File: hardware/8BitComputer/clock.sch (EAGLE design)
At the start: 28 parts, among them IC1 LM555CN, J1 Power, J2 Power, Q1 P2N2222AZL1G, Q2 P2N2222AZL1G

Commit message: lay out for size of our FR-4 boards
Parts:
- added U$3: CMD_C0DE_LOGOCMD_CODE_LOGO_TOP_COPPER, logos:CMD_C0DE_LOGOCMD_CODE_LOGO_TOP_COPPER
- C2: device passives:C-USC0805 -> passives:C-US075-032X103
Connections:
- net GND: now also LED2.C; no longer R6.2
- net MANUAL_TIMER: now also R6.1; no longer LED2.A
- net N$5: now also LED2.A, R6.2; no longer LED2.C, R6.1
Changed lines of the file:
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@@
 <layers>
 <layer number="1" name="Top" color="4" fill="1" visible="no" active="no"/>
-<layer number="2" name="Route2" color="1" fill="3" visible="no" active="no"/>
-<layer number="3" name="Route3" color="4" fill="3" visible="no" active="no"/>
-<layer number="4" name="Route4" color="1" fill="4" visible="no" active="no"/>
-<layer number="5" name="Route5" color="4" fill="4" visible="no" active="no"/>
-<layer number="6" name="Route6" color="1" fill="8" visible="no" active="no"/>
-<layer number="7" name="Route7" color="4" fill="8" visible="no" active="no"/>
-<layer number="8" name="Route8" color="1" fill="2" visible="no" active="no"/>
-<layer number="9" name="Route9" color="4" fill="2" visible="no" active="no"/>
-<layer number="10" name="Route10" color="1" fill="7" visible="no" active="no"/>
-<layer number="11" name="Route11" color="4" fill="7" visible="no" active="no"/>
-<layer number="12" name="Route12" color="1" fill="5" visible="no" active="no"/>
-<layer number="13" name="Route13" color="4" fill="5" visible="no" active="no"/>
-<layer number="14" name="Route14" color="1" fill="6" visible="no" active="no"/>
-<layer number="15" name="Route15" color="4" fill="6" visible="no" active="no"/>
+<layer number="2" name="Route2" color="16" fill="1" visible="no" active="no"/>
+<layer number="3" name="Route3" color="17" fill="1" visible="no" active="no"/>
+<layer number="4" name="Route4" color="18" fill="1" visible="no" active="no"/>
+<layer number="5" name="Route5" color="19" fill="1" visible="no" active="no"/>
+<layer number="6" name="Route6" color="25" fill="1" visible="no" active="no"/>
+<layer number="7" name="Route7" color="26" fill="1" visible="no" active="no"/>
+<layer number="8" name="Route8" color="27" fill="1" visible="no" active="no"/>
+<layer number="9" name="Route9" color="28" fill="1" visible="no" active="no"/>
+<layer number="10" name="Route10" color="29" fill="1" visible="no" active="no"/>
+<layer number="11" name="Route11" color="30" fill="1" visible="no" active="no"/>
+<layer number="12" name="Route12" color="20" fill="1" visible="no" active="no"/>
+<layer number="13" name="Route13" color="21" fill="1" visible="no" active="no"/>
+<layer number="14" name="Route14" color="22" fill="1" visible="no" active="no"/>
+<layer number="15" name="Route15" color="23" fill="1" visible="no" active="no"/>
 <layer number="16" name="Bottom" color="1" fill="1" visible="no" active="no"/>
 <layer number="17" name="Pads" color="2" fill="1" visible="no" active="no"/>
 <layer number="18" name="Vias" color="2" fill="1" visible="no" active="no"/>
 <layer number="19" name="Unrouted" color="6" fill="1" visible="no" active="no"/>
-<layer number="20" name="Dimension" color="15" fill="1" visible="no" active="no"/>
+<layer number="20" name="Dimension" color="24" fill="1" visible="no" active="no"/>
 <layer number="21" name="tPlace" color="7" fill="1" visible="no" active="no"/>
 <layer number="22" name="bPlace" color="7" fill="1" visible="no" active="no"/>
@@
 <part name="U$1" library="passives" deviceset="SQUARE-TRIMPOT-POTENTIOMETER" device=""/>
 <part name="R2" library="passives" deviceset="RESISTOR" device="0805-RES" value="1 K"/>
-<part name="C2" library="passives" deviceset="C-US" device="C0805" value="100 nF"/>
+<part name="C2" library="passives" deviceset="C-US" device="075-032X103" value="100 nF"/>
 <part name="C3" library="passives" deviceset="C-US" device="C0805" value="1 uF"/>
 <part name="R3" library="passives" deviceset="RESISTOR" device="0805-RES" value="1 K"/>
@@
 <part name="J3" library="connector" deviceset="M08" device="SILK_FEMALE_PTH"/>
 <part name="J2" library="connector" deviceset="M02" device="PTH" value="Power"/>
+<part name="U$3" library="logos" deviceset="CMD_C0DE_LOGO" device="CMD_CODE_LOGO_TOP_COPPER"/>
 </parts>
 <sheets>
@@
 <attribute name="VALUE" x="39.116" y="56.769" size="1.778" layer="96"/>
 </instance>
-<instance part="LED2" gate="G$1" x="45.72" y="71.12" smashed="yes" rot="R180">
-<attribute name="NAME" x="42.164" y="75.692" size="1.778" layer="95" rot="R270"/>
-<attribute name="VALUE" x="50.165" y="75.692" size="1.778" layer="96" rot="R270"/>
-</instance>
-<instance part="R6" gate="G$1" x="45.72" y="83.82" smashed="yes" rot="R90">
-<attribute name="NAME" x="44.2214" y="80.01" size="1.778" layer="95" rot="R90"/>
-<attribute name="VALUE" x="49.022" y="80.01" size="1.778" layer="96" rot="R90"/>
+<instance part="LED2" gate="G$1" x="45.72" y="86.36" smashed="yes" rot="R180">
+<attribute name="NAME" x="42.164" y="90.932" size="1.778" layer="95" rot="R270"/>
+<attribute name="VALUE" x="50.165" y="90.932" size="1.778" layer="96" rot="R270"/>
+</instance>
+<instance part="R6" gate="G$1" x="45.72" y="73.66" smashed="yes" rot="R90">
+<attribute name="NAME" x="44.2214" y="69.85" size="1.778" layer="95" rot="R90"/>
+<attribute name="VALUE" x="49.022" y="69.85" size="1.778" layer="96" rot="R90"/>
 </instance>
 </instances>
@@
 <junction x="38.1" y="63.5"/>
 <label x="50.8" y="63.5" size="1.778" layer="95"/>
-<pinref part="LED2" gate="G$1" pin="A"/>
+<pinref part="R6" gate="G$1" pin="1"/>
 <wire x1="45.72" y1="63.5" x2="50.8" y2="63.5" width="0.1524" layer="91"/>
 <wire x1="45.72" y1="68.58" x2="45.72" y2="63.5" width="0.1524" layer="91"/>
@@
 </segment>
 <segment>
+<pinref part="LED2" gate="G$1" pin="C"/>
+<wire x1="45.72" y1="91.44" x2="45.72" y2="93.98" width="0.1524" layer="91"/>
+<label x="45.72" y="93.98" size="1.778" layer="95"/>
+</segment>
+</net>
+<net name="N$5" class="0">
+<segment>
 <pinref part="R6" gate="G$1" pin="2"/>
-<wire x1="45.72" y1="88.9" x2="45.72" y2="91.44" width="0.1524" layer="91"/>
-<label x="45.72" y="91.44" size="1.778" layer="95"/>
-</segment>
-</net>
-<net name="N$5" class="0">
-<segment>
-<pinref part="LED2" gate="G$1" pin="C"/>
-<pinref part="R6" gate="G$1" pin="1"/>
-<wire x1="45.72" y1="76.2" x2="45.72" y2="78.74" width="0.1524" layer="91"/>
+<pinref part="LED2" gate="G$1" pin="A"/>
+<wire x1="45.72" y1="78.74" x2="45.72" y2="83.82" width="0.1524" layer="91"/>
 </segment>
 </net>
@@
 </nets>
 </sheet>
+<sheet>
+<plain>
+</plain>
+<instances>
+<instance part="U$3" gate="G$1" x="40.64" y="63.5" smashed="yes"/>
+</instances>
+<busses>
+</busses>
+<nets>
+</nets>
+</sheet>

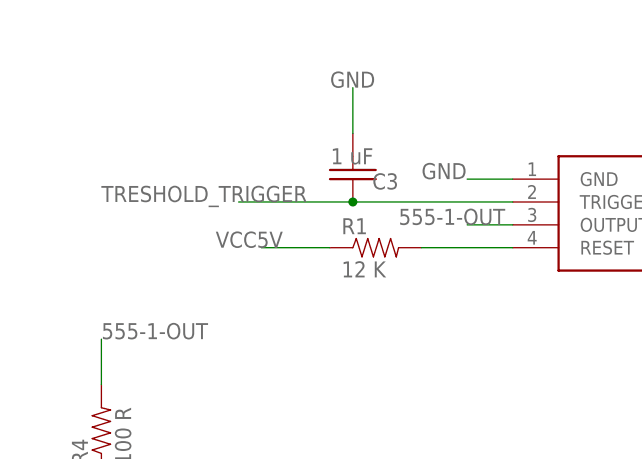
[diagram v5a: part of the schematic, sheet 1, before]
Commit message: fixed missing trace on 555- miss spelled threshold :(
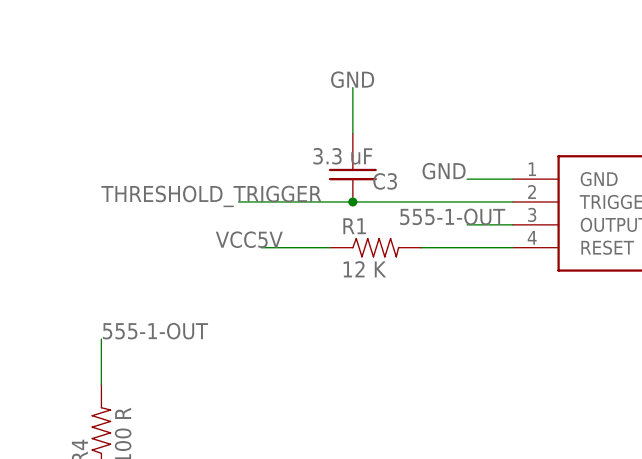
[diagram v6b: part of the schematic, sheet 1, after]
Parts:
- C3: value 1 uF -> 3.3 uF
- J3: value (none) -> CLK_OUTS
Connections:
- removed net TRESHOLD_TRIGGER: C3.1, IC1.TRIGGER
- net THRESHOLD_TRIGGER: now also C3.1, IC1.TRIGGER
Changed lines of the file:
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@@
 <part name="R2" library="passives" deviceset="RESISTOR" device="0805-RES" value="1 K"/>
 <part name="C2" library="passives" deviceset="C-US" device="075-032X103" value="100 nF"/>
-<part name="C3" library="passives" deviceset="C-US" device="C0805" value="1 uF"/>
+<part name="C3" library="passives" deviceset="C-US" device="C0805" value="3.3 uF"/>
 <part name="R3" library="passives" deviceset="RESISTOR" device="0805-RES" value="1 K"/>
 <part name="LED1" library="leds" deviceset="LED" device="-3MM-NO_SILK" value="Blue"/>
@@
 <part name="R9" library="passives" deviceset="RESISTOR" device="0805-RES" value="1 K"/>
 <part name="C6" library="passives" deviceset="C-US" device="C0805" value="0.1 uF"/>
-<part name="J3" library="connector" deviceset="M08" device="SILK_FEMALE_PTH"/>
+<part name="J3" library="connector" deviceset="M08" device="SILK_FEMALE_PTH" value="CLK_OUTS"/>
 <part name="J2" library="connector" deviceset="M02" device="PTH" value="Power"/>
 <part name="U$3" library="logos" deviceset="CMD_C0DE_LOGO" device="CMD_CODE_LOGO_TOP_COPPER"/>
@@
 <label x="71.12" y="30.48" size="1.778" layer="95"/>
 </segment>
+<segment>
+<pinref part="IC1" gate="G$1" pin="TRIGGER"/>
+<pinref part="C3" gate="G$1" pin="1"/>
+<wire x1="12.7" y1="58.42" x2="-5.08" y2="58.42" width="0.1524" layer="91"/>
+<wire x1="-5.08" y1="58.42" x2="-17.78" y2="58.42" width="0.1524" layer="91"/>
+<junction x="-5.08" y="58.42"/>
+<label x="-33.02" y="58.42" size="1.778" layer="95"/>
+</segment>
 </net>
 <net name="VCC5V" class="0">
@@
 <wire x1="66.04" y1="53.34" x2="71.12" y2="53.34" width="0.1524" layer="91"/>
 <junction x="66.04" y="53.34"/>
-</segment>
-</net>
-<net name="TRESHOLD_TRIGGER" class="0">
-<segment>
-<pinref part="IC1" gate="G$1" pin="TRIGGER"/>
-<pinref part="C3" gate="G$1" pin="1"/>
-<wire x1="12.7" y1="58.42" x2="-5.08" y2="58.42" width="0.1524" layer="91"/>
-<wire x1="-5.08" y1="58.42" x2="-17.78" y2="58.42" width="0.1524" layer="91"/>
-<junction x="-5.08" y="58.42"/>
-<label x="-33.02" y="58.42" size="1.778" layer="95"/>
 </segment>
 </net>
@@
 </instance>
 <instance part="J3" gate="G$1" x="165.1" y="25.4" smashed="yes" rot="R180">
-<attribute name="VALUE" x="170.18" y="38.1" size="1.778" layer="96" rot="R180"/>
+<attribute name="VALUE" x="170.18" y="40.64" size="1.778" layer="96" rot="R180"/>
 <attribute name="NAME" x="170.18" y="11.938" size="1.778" layer="95" rot="R180"/>
 </instance>

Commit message: updated clock to be a bit easier to solder by using bottom layer more. Thought here is that if the hole through pin only needs connection on one side then it should be the bottom so I don't have to solder both top and bottom of each pin
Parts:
- R5: device passives:RESISTOR0805-RES -> passives:RESISTORAXIAL-0.3
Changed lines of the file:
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@@
 <?xml version="1.0" encoding="utf-8"?>
 <!DOCTYPE eagle SYSTEM "eagle.dtd">
-<eagle version="9.3.2">
+<eagle version="9.4.0">
 <drawing>
 <settings>
@@
 <grid distance="0.1" unitdist="inch" unit="inch" style="lines" multiple="1" display="no" altdistance="0.01" altunitdist="inch" altunit="inch"/>
 <layers>
-<layer number="1" name="Top" color="4" fill="1" visible="no" active="no"/>
-<layer number="2" name="Route2" color="16" fill="1" visible="no" active="no"/>
-<layer number="3" name="Route3" color="17" fill="1" visible="no" active="no"/>
-<layer number="4" name="Route4" color="18" fill="1" visible="no" active="no"/>
-<layer number="5" name="Route5" color="19" fill="1" visible="no" active="no"/>
-<layer number="6" name="Route6" color="25" fill="1" visible="no" active="no"/>
-<layer number="7" name="Route7" color="26" fill="1" visible="no" active="no"/>
-<layer number="8" name="Route8" color="27" fill="1" visible="no" active="no"/>
-<layer number="9" name="Route9" color="28" fill="1" visible="no" active="no"/>
-<layer number="10" name="Route10" color="29" fill="1" visible="no" active="no"/>
-<layer number="11" name="Route11" color="30" fill="1" visible="no" active="no"/>
-<layer number="12" name="Route12" color="20" fill="1" visible="no" active="no"/>
-<layer number="13" name="Route13" color="21" fill="1" visible="no" active="no"/>
-<layer number="14" name="Route14" color="22" fill="1" visible="no" active="no"/>
-<layer number="15" name="Route15" color="23" fill="1" visible="no" active="no"/>
-<layer number="16" name="Bottom" color="1" fill="1" visible="no" active="no"/>
-<layer number="17" name="Pads" color="2" fill="1" visible="no" active="no"/>
-<layer number="18" name="Vias" color="2" fill="1" visible="no" active="no"/>
-<layer number="19" name="Unrouted" color="6" fill="1" visible="no" active="no"/>
-<layer number="20" name="Dimension" color="24" fill="1" visible="no" active="no"/>
-<layer number="21" name="tPlace" color="7" fill="1" visible="no" active="no"/>
-<layer number="22" name="bPlace" color="7" fill="1" visible="no" active="no"/>
-<layer number="23" name="tOrigins" color="15" fill="1" visible="no" active="no"/>
-<layer number="24" name="bOrigins" color="15" fill="1" visible="no" active="no"/>
-<layer number="25" name="tNames" color="7" fill="1" visible="no" active="no"/>
-<layer number="26" name="bNames" color="7" fill="1" visible="no" active="no"/>
-<layer number="27" name="tValues" color="7" fill="1" visible="no" active="no"/>
-<layer number="28" name="bValues" color="7" fill="1" visible="no" active="no"/>
+<layer number="1" name="Top" color="4" fill="1" visible="yes" active="no"/>
+<layer number="2" name="Route2" color="16" fill="1" visible="yes" active="no"/>
+<layer number="3" name="Route3" color="17" fill="1" visible="yes" active="no"/>
+<layer number="4" name="Route4" color="18" fill="1" visible="yes" active="no"/>
+<layer number="5" name="Route5" color="19" fill="1" visible="yes" active="no"/>
+<layer number="6" name="Route6" color="25" fill="1" visible="yes" active="no"/>
+<layer number="7" name="Route7" color="26" fill="1" visible="yes" active="no"/>
+<layer number="8" name="Route8" color="27" fill="1" visible="yes" active="no"/>
+<layer number="9" name="Route9" color="28" fill="1" visible="yes" active="no"/>
+<layer number="10" name="Route10" color="29" fill="1" visible="yes" active="no"/>
+<layer number="11" name="Route11" color="30" fill="1" visible="yes" active="no"/>
+<layer number="12" name="Route12" color="20" fill="1" visible="yes" active="no"/>
+<layer number="13" name="Route13" color="21" fill="1" visible="yes" active="no"/>
+<layer number="14" name="Route14" color="22" fill="1" visible="yes" active="no"/>
+<layer number="15" name="Route15" color="23" fill="1" visible="yes" active="no"/>
+<layer number="16" name="Bottom" color="1" fill="1" visible="yes" active="no"/>
+<layer number="17" name="Pads" color="2" fill="1" visible="yes" active="no"/>
+<layer number="18" name="Vias" color="2" fill="1" visible="yes" active="no"/>
+<layer number="19" name="Unrouted" color="6" fill="1" visible="yes" active="no"/>
+<layer number="20" name="Dimension" color="24" fill="1" visible="yes" active="no"/>
+<layer number="21" name="tPlace" color="7" fill="1" visible="yes" active="no"/>
+<layer number="22" name="bPlace" color="7" fill="1" visible="yes" active="no"/>
+<layer number="23" name="tOrigins" color="15" fill="1" visible="yes" active="no"/>
+<layer number="24" name="bOrigins" color="15" fill="1" visible="yes" active="no"/>
+<layer number="25" name="tNames" color="7" fill="1" visible="yes" active="no"/>
+<layer number="26" name="bNames" color="7" fill="1" visible="yes" active="no"/>
+<layer number="27" name="tValues" color="7" fill="1" visible="yes" active="no"/>
+<layer number="28" name="bValues" color="7" fill="1" visible="yes" active="no"/>
 <layer number="29" name="tStop" color="7" fill="3" visible="no" active="no"/>
 <layer number="30" name="bStop" color="7" fill="6" visible="no" active="no"/>
@@
 <layer number="35" name="tGlue" color="7" fill="4" visible="no" active="no"/>
 <layer number="36" name="bGlue" color="7" fill="5" visible="no" active="no"/>
-<layer number="37" name="tTest" color="7" fill="1" visible="no" active="no"/>
-<layer number="38" name="bTest" color="7" fill="1" visible="no" active="no"/>
+<layer number="37" name="tTest" color="7" fill="1" visible="yes" active="no"/>
+<layer number="38" name="bTest" color="7" fill="1" visible="yes" active="no"/>
 <layer number="39" name="tKeepout" color="4" fill="11" visible="no" active="no"/>
 <layer number="40" name="bKeepout" color="1" fill="11" visible="no" active="no"/>
@@
 <layer number="44" name="Drills" color="7" fill="1" visible="no" active="no"/>
 <layer number="45" name="Holes" color="7" fill="1" visible="no" active="no"/>
-<layer number="46" name="Milling" color="3" fill="1" visible="no" active="no"/>
-<layer number="47" name="Measures" color="7" fill="1" visible="no" active="no"/>
-<layer number="48" name="Document" color="7" fill="1" visible="no" active="no"/>
-<layer number="49" name="Reference" color="7" fill="1" visible="no" active="no"/>
-<layer number="50" name="dxf" color="7" fill="1" visible="no" active="no"/>
-<layer number="51" name="tDocu" color="7" fill="1" visible="no" active="no"/>
-<layer number="52" name="bDocu" color="7" fill="1" visible="no" active="no"/>
-<layer number="53" name="tGND_GNDA" color="7" fill="9" visible="no" active="no"/>
-<layer number="54" name="bGND_GNDA" color="1" fill="9" visible="no" active="no"/>
-<layer number="56" name="wert" color="7" fill="1" visible="no" active="no"/>
-<layer number="57" name="tCAD" color="7" fill="1" visible="no" active="no"/>
-<layer number="59" name="tCarbon" color="7" fill="1" visible="no" active="no"/>
-<layer number="60" name="bCarbon" color="7" fill="1" visible="no" active="no"/>
+<layer number="46" name="Milling" color="3" fill="1" visible="yes" active="no"/>
+<layer number="47" name="Measures" color="7" fill="1" visible="yes" active="no"/>
+<layer number="48" name="Document" color="7" fill="1" visible="yes" active="no"/>
+<layer number="49" name="Reference" color="7" fill="1" visible="yes" active="no"/>
+<layer number="50" name="dxf" color="7" fill="1" visible="yes" active="no"/>
+<layer number="51" name="tDocu" color="7" fill="1" visible="yes" active="no"/>
+<layer number="52" name="bDocu" color="7" fill="1" visible="yes" active="no"/>
+<layer number="53" name="tGND_GNDA" color="7" fill="9" visible="yes" active="no"/>
+<layer number="54" name="bGND_GNDA" color="1" fill="9" visible="yes" active="no"/>
+<layer number="56" name="wert" color="7" fill="1" visible="yes" active="no"/>
+<layer number="57" name="tCAD" color="7" fill="1" visible="yes" active="no"/>
+<layer number="59" name="tCarbon" color="7" fill="1" visible="yes" active="no"/>
+<layer number="60" name="bCarbon" color="7" fill="1" visible="yes" active="no"/>
 <layer number="88" name="SimResults" color="9" fill="1" visible="yes" active="yes"/>
 <layer number="89" name="SimProbes" color="9" fill="1" visible="yes" active="yes"/>
@@
 <part name="J1" library="connector" deviceset="M02" device="PTH" value="Power"/>
 <part name="U$2" library="switches" deviceset="SWITCH_TACTILE" device="TACTILE_PIN"/>
-<part name="R5" library="passives" deviceset="RESISTOR" device="0805-RES" value="4.7 K"/>
+<part name="R5" library="passives" deviceset="RESISTOR" device="AXIAL-0.3" value="4.7 K"/>
 <part name="C4" library="passives" deviceset="C-US" device="C0805" value="0.1 uF"/>
 <part name="S1" library="switches" deviceset="SWITCH-SPST" device="KIT" value="555 or Manual"/>
